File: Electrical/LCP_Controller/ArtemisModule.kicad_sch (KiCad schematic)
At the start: 14 parts, among them J11 Tag-Connect SWD, SW1 RESET, U12 Artemis_Module, Y1 32.768KHz

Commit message: Hardware Revision : v0.3
1. modified schematic design, removed unnecessary test points.
2. pcb layout 2x8 Inches allowance dimension, layout is in progress
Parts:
- removed TP13: 5002, TestPoint:TestPoint_Keystone_5000-5004_Miniature, symbol Connector:TestPoint
- added H1, H2, H3, H4: MountingHole_Pad, MountingHole:MountingHole_2.5mm_Pad, symbol Mechanical:MountingHole_Pad
- added RN3, RN4: 2k2, Resistor_SMD:R_Array_Concave_2x0603, symbol Device:R_Pack02
- renumbered C51 to C15, C52 to C16, C41 to C17, C42 to C18, C43 to C19, C39 to C20, C40 to C21, J11 to J4, R33 to R17, RN4 to RN2, U12 to U4
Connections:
- net +3.3V: now also RN3.1 (R1.1), RN3.2 (R2.1), RN4.1 (R1.1), RN4.2 (R2.1)
- net ARTEMIS_D39_SCL(4): now also RN4.4 (R1.2)
- net ARTEMIS_D40_SDA(4): now also RN4.3 (R2.2)
- net ARTEMIS_D8_SCL(1): now also RN3.3 (R2.2)
- net ARTEMIS_D9_SDA(1): now also RN3.4 (R1.2)
- net GND: now also H1.1, H2.1, H3.1, H4.1
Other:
- note added: "I2C Interface"
- note added: "I2C_1"
- note added: "I2C_2"
- note added: "I2C_4"
- note added: "Mounting Holes for the PCB"
- note added: "SPI Interface"
- note added: "SPI-0"
- note added: "SPI-3"
- note added: "UART Interface"
- note added: "UART_1"
- note added: "changed series cap (C15) from 1nF to 0.1uF"
- note removed: "changed series cap (C51) from 1nF to 0.1uF"

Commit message: Hw Rev : 0.3v
changed buck-coverter LMR50410XDBVR to BD9G102G-LB, added schotty diode.
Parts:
- C15: footprint Capacitor_SMD:C_0603_1608Metric -> Capacitor_SMD:C_0805_2012Metric; MPN C0603X102J4RECAUTO -> 885012207016
- RN2, RN3, RN4: MPN EXB-V4V103JV -> EXB-V4V222JV
- Y1: MPN ECS-.327-12.5-34B-TR -> ECS-.327-12.5-34R-TR

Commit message: Hw Rev : 0.3v updated
changed TRS3122ERGER to TRS3122ERGET due to shortage of part.
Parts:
- H1, H2, H3, H4: Population (none) -> DNP

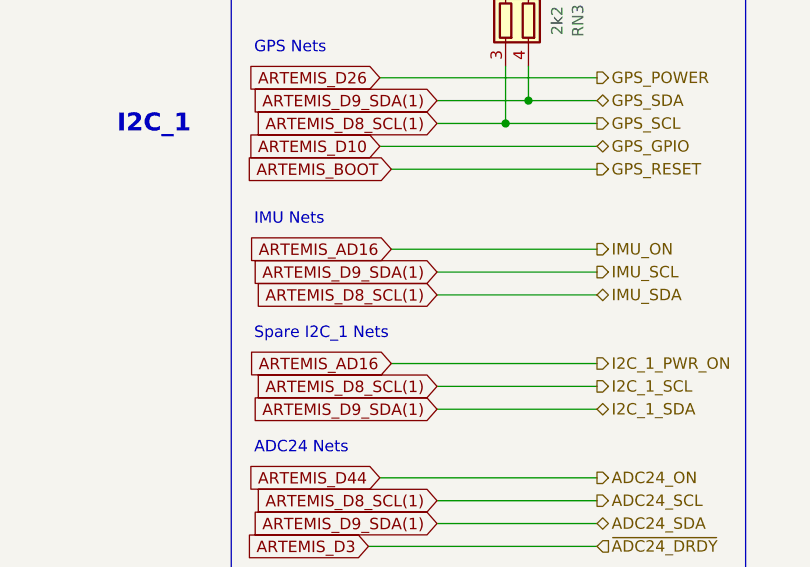
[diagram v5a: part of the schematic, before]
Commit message: GPS and Iridium Layout Finalized
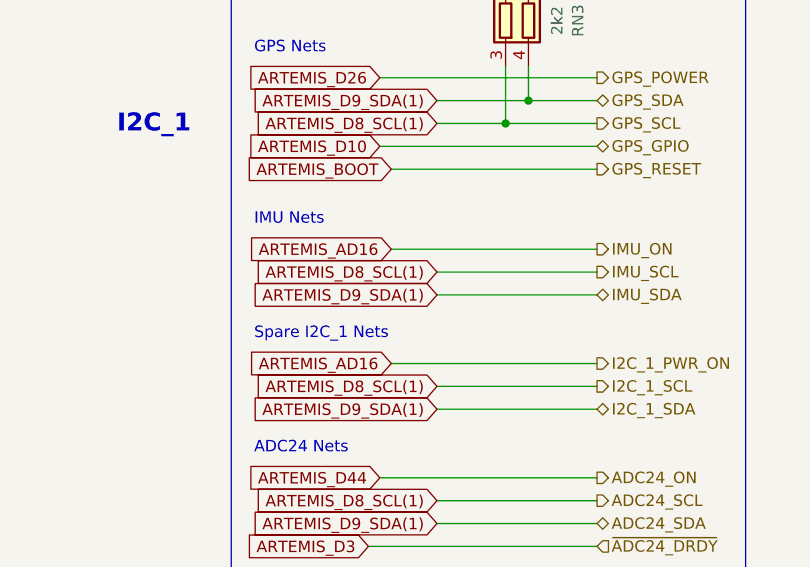
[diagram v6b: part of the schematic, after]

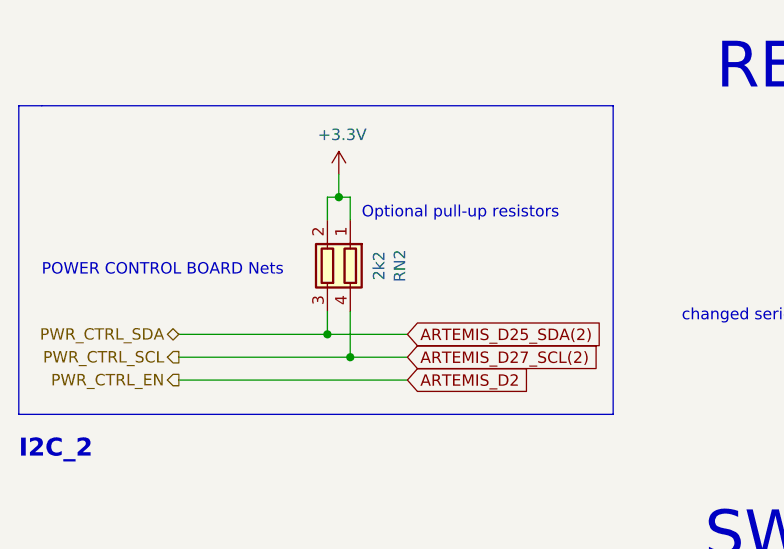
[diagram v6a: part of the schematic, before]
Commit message: Completed Board Mods
COM 0, 1, 2, 3 are now microfit.

Control Board I2C Interconnect

Separated from PWR and now microfit.

RN2 changed to 4k7.

J3, J9, J12, J16 are removed.

U8 circuit moved under IMU footprint.

C11 and C13 moved between IMU and Iridium.

GPS moved from underneath Iridium.
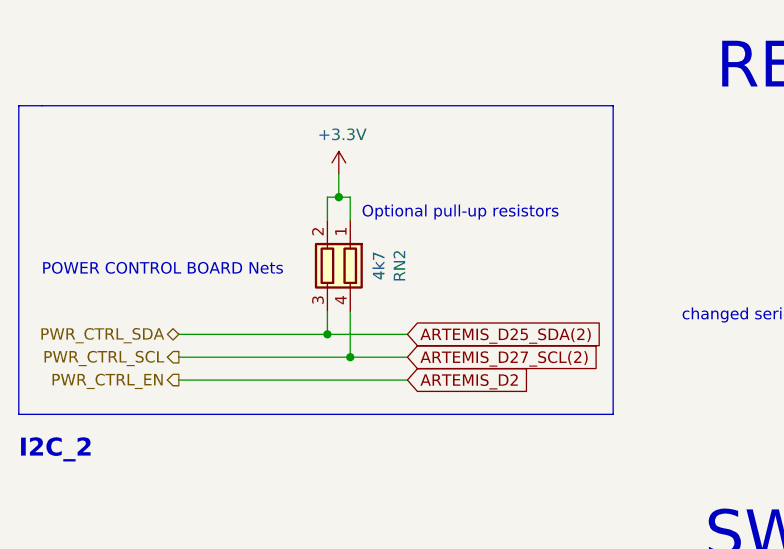
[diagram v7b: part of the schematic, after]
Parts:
- RN2: value 2k2 -> 4k7
